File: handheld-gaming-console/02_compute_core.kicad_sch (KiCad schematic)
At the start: 2 parts, among them J3 CM4_MAIN, J4 CM4_PERIPH

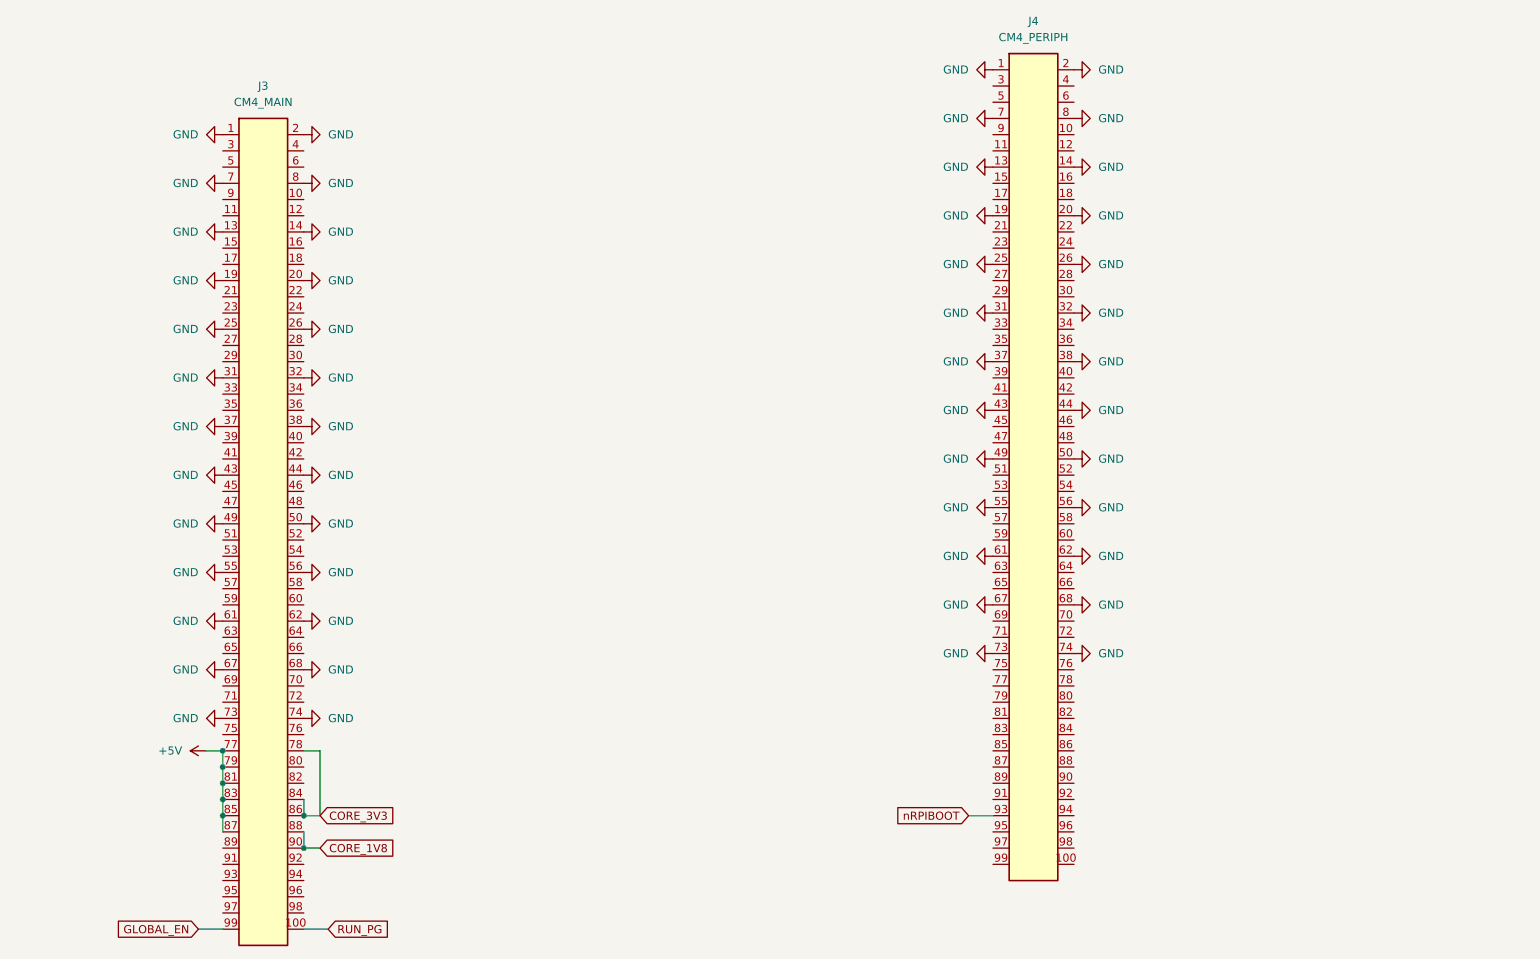
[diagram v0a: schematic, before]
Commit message: feat(usb): implement TS3USB221A high-speed mux, recovery switch, and otg role switching
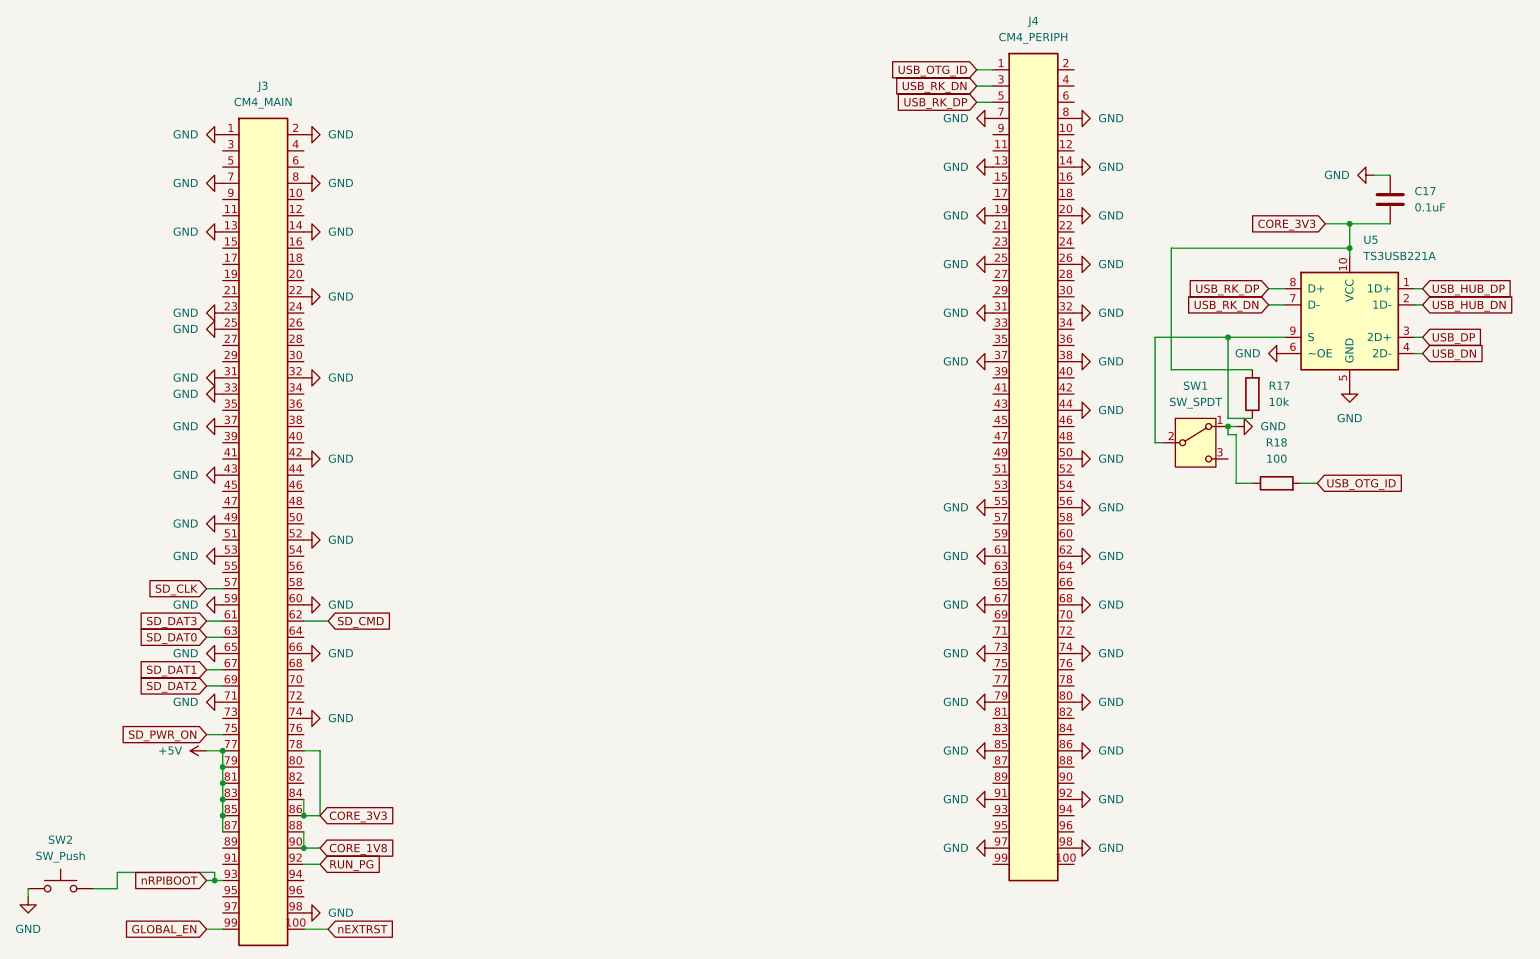
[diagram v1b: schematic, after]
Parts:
- added C17: 0.1uF, symbol Device:C
- added R17: 10k, symbol Device:R
- added R18: 100, symbol Device:R
- added SW1: SW_SPDT, Button_Switch_SMD:SW_SPDT_PCM12, symbol Switch:SW_SPDT
- added SW2: SW_Push, Button_Switch_SMD:SW_Push_SPST_NO_Alps_SKRK, symbol Switch:SW_Push
- added U5: TS3USB221A, Package_DFN_QFN:UQFN-10_1.6x2.1mm_P0.5mm, symbol custom-components:TS3USB221A
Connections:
- net CORE_3V3: now also C17.2, R17.2, U5.10 (VCC)
- net GND: now also J3.22 (Pin_22), J3.23 (Pin_23), J3.33 (Pin_33), J3.42 (Pin_42), J3.52 (Pin_52), J3.53 (Pin_53), J3.59 (Pin_59), J3.60 (Pin_60), J3.65 (Pin_65), J3.66 (Pin_66), J3.71 (Pin_71), J3.98 (Pin_98), J4.79 (Pin_79), J4.80 (Pin_80), J4.85 (Pin_85), J4.86 (Pin_86), J4.91 (Pin_91), J4.92 (Pin_92), J4.97 (Pin_97), J4.98 (Pin_98), C17.1, R18.1, SW1.1 (A), SW2.1, U5.5 (GND), U5.6 (~OE); no longer J3.19 (Pin_19), J3.20 (Pin_20), J3.26 (Pin_26), J3.38 (Pin_38), J3.44 (Pin_44), J3.50 (Pin_50), J3.55 (Pin_55), J3.56 (Pin_56), J3.61 (Pin_61), J3.62 (Pin_62), J3.67 (Pin_67), J3.68 (Pin_68), J3.73 (Pin_73), J4.1 (Pin_1), J4.2 (Pin_2), J4.43 (Pin_43), J4.49 (Pin_49)
- net RUN_PG: now also J3.92 (Pin_92); no longer J3.100 (Pin_100)
- net nRPIBOOT: now also J3.93 (Pin_93), SW2.2; no longer J4.93 (Pin_93)
- net USB_RK_DN: now reaches J4.3 (Pin_3)
- net USB_RK_DN: now also U5.7 (D-)
- net USB_RK_DP: now reaches J4.5 (Pin_5)
- net USB_RK_DP: now also U5.8 (D+)
- net SD_CLK: now reaches J3.57 (Pin_57)
- net SD_DAT0: now reaches J3.63 (Pin_63)
- net SD_DAT2: now reaches J3.69 (Pin_69)
- net SD_PWR_ON: now reaches J3.75 (Pin_75)
- new net: R17.1, SW1.2 (B), U5.9 (S)
- new net SD_CMD: J3.62 (Pin_62)
- new net SD_DAT1: J3.67 (Pin_67)
- new net SD_DAT3: J3.61 (Pin_61)
- new net USB_DN: U5.4 (2D-)
- new net USB_DP: U5.3 (2D+)
- new net USB_HUB_DN: U5.2 (1D-)
- new net USB_HUB_DP: U5.1 (1D+)
- new net USB_OTG_ID: J4.1 (Pin_1), R18.2
- new net nEXTRST: J3.100 (Pin_100)

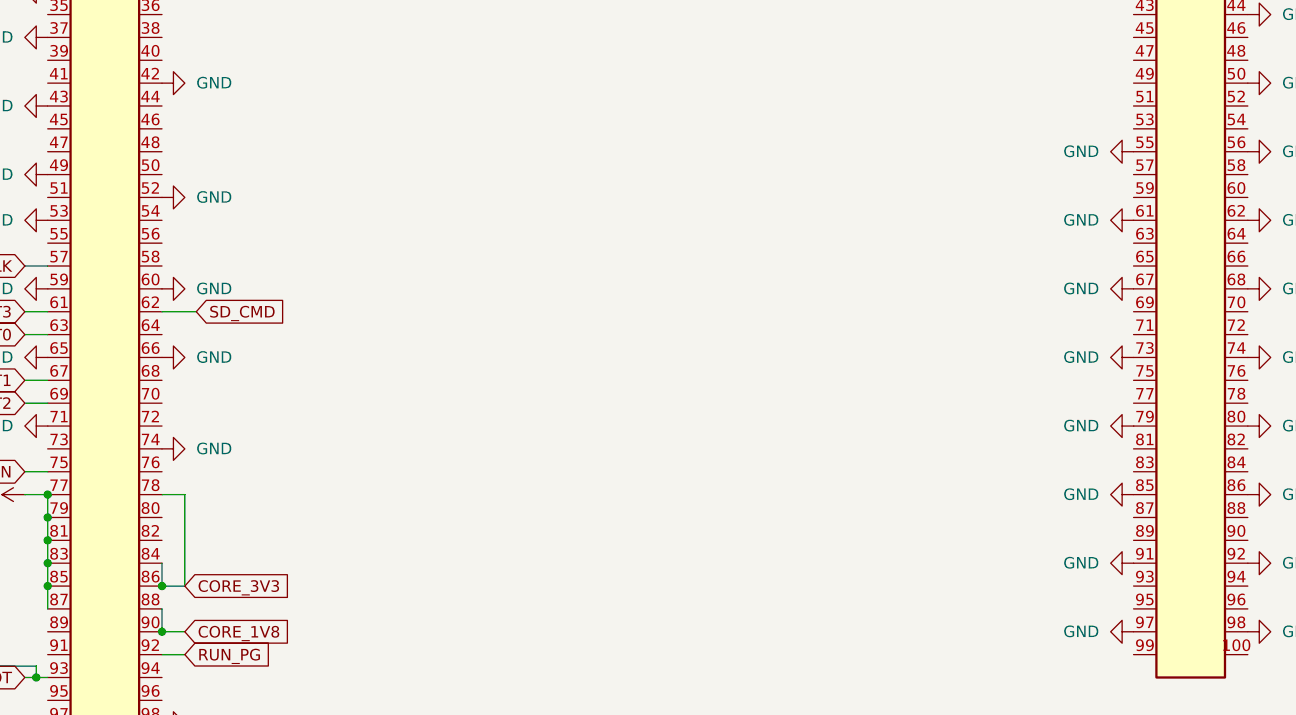
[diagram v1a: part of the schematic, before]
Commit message: feat(display): wire 15-pin FPC connector with MIPI-DSI lanes and touch I2C bus
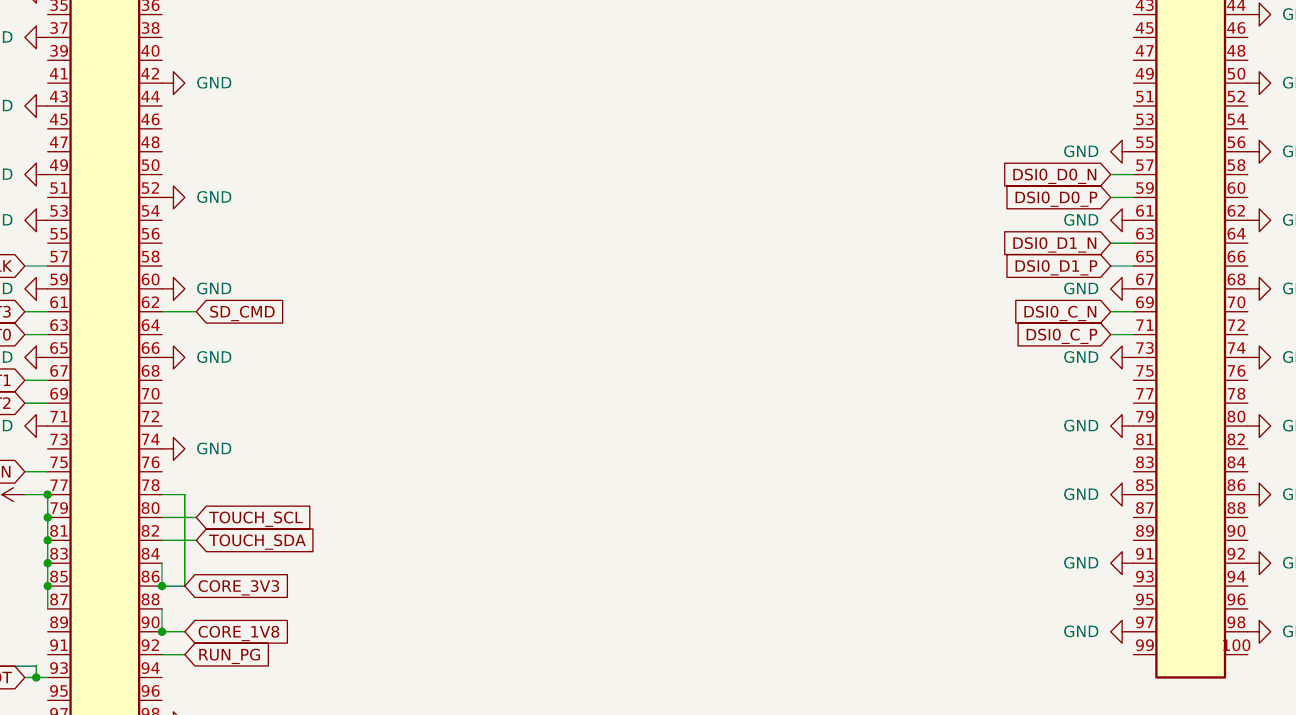
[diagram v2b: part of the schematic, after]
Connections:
- net DSI0_D0_N: now reaches J4.57 (Pin_57)
- net DSI0_D0_P: now reaches J4.59 (Pin_59)
- net DSI0_D1_N: now reaches J4.63 (Pin_63)
- net DSI0_D1_P: now reaches J4.65 (Pin_65)
- net DSI0_C_N: now reaches J4.69 (Pin_69)
- net DSI0_C_P: now reaches J4.71 (Pin_71)
- net TOUCH_SCL: now reaches J3.80 (Pin_80)
- net TOUCH_SDA: now reaches J3.82 (Pin_82)

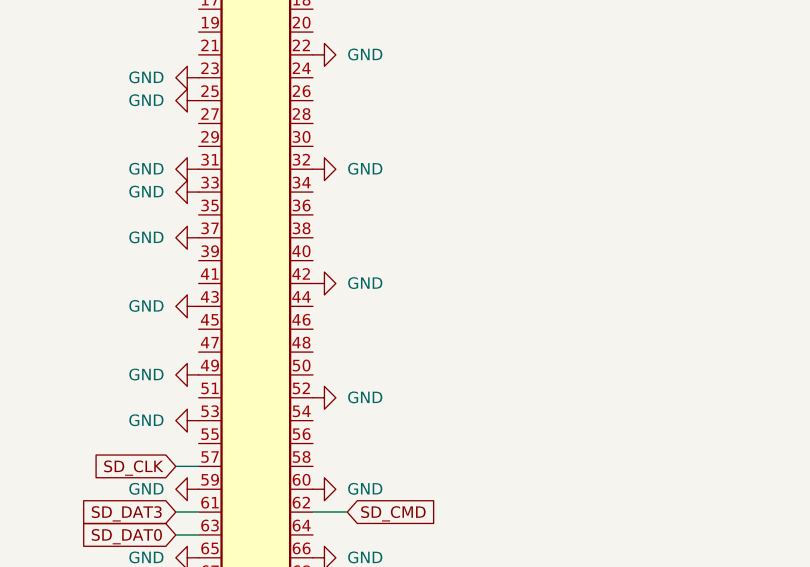
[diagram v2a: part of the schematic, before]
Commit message: feat(display): implement 3V3_LCD power switch and GT911 I2C pull-ups with address strap
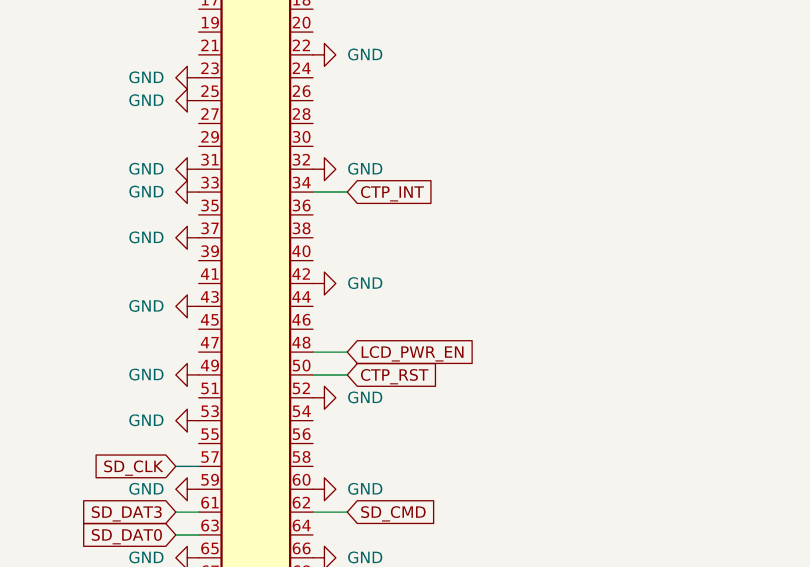
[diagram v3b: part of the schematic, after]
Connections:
- net CTP_INT: now reaches J3.34 (Pin_34)
- net LCD_PWR_EN: now reaches J3.48 (Pin_48)
- net CTP_RST: now reaches J3.50 (Pin_50)
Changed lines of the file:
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@@
+	(wire
+		(pts
+			(xy 87.63 96.52) (xy 91.44 96.52)
+		)
+		(stroke
+			(width 0)
+			(type default)
+		)
+	)
 	(wire
 		(pts
@@
 	(wire
 		(pts
+			(xy 87.63 78.74) (xy 91.44 78.74)
+		)
+		(stroke
+			(width 0)
+			(type default)
+		)
+	)
+	(wire
+		(pts
 			(xy 87.63 114.3) (xy 91.44 114.3)
 		)
@@
 	(wire
 		(pts
+			(xy 87.63 99.06) (xy 91.44 99.06)
+		)
+		(stroke
+			(width 0)
+			(type default)
+		)
+	)
+	(wire
+		(pts
 			(xy 223.52 74.93) (xy 223.52 55.88)
 		)
@@
 		)
 	)
+	(global_label "CTP_INT"
+		(shape input)
+		(at 91.44 78.74 0)
+		(fields_autoplaced yes)
+		(effects
+			(font
+				(size 1.27 1.27)
+			)
+			(justify left)
+		)
+		(property "Intersheetrefs" "${INTERSHEET_REFS}"
+			(at 101.8033 78.74 0)
+			(hide yes)
+			(show_name no)
+			(do_not_autoplace no)
+			(effects
+				(font
+					(size 1.27 1.27)
+				)
+				(justify left)
+			)
+		)
+	)
 	(global_label "CORE_3V3"
 		(shape input)
@@
 		)
 	)
+	(global_label "CTP_RST"
+		(shape input)
+		(at 91.44 99.06 0)
+		(fields_autoplaced yes)
+		(effects
+			(font
+				(size 1.27 1.27)
+			)
+			(justify left)
+		)
+		(property "Intersheetrefs" "${INTERSHEET_REFS}"
+			(at 102.3475 99.06 0)
+			(hide yes)
+			(show_name no)
+			(do_not_autoplace no)
+			(effects
+				(font
+					(size 1.27 1.27)
+				)
+				(justify left)
+			)
+		)
+	)
 	(global_label "DSI0_C_P"
 		(shape input)
@@
 			(hide yes)
 			(show_name no)
+			(do_not_autoplace no)
+			(effects
+				(font
+					(size 1.27 1.27)
+				)
+				(justify left)
+			)
+		)
+	)
+	(global_label "LCD_PWR_EN"
+		(shape input)
+		(at 91.44 96.52 0)
+		(fields_autoplaced yes)
+		(effects
+			(font
+				(size 1.27 1.27)
+			)
+			(justify left)
+		)
+		(property "Intersheetrefs" "${INTERSHEET_REFS}"
+			(at 106.3994 96.52 0)
+			(hide yes)
+			(show_name no)

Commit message: fix(core): correct J3 ground matrix, fix UART pins, add OTG_ID pull-up, and reduce BQ24075 input capacitance per design audit
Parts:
- added R33: 10k, symbol Device:R
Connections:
- net CORE_3V3: now also R33.2
- net GND: no longer J3.25 (Pin_25), J3.31 (Pin_31), J3.37 (Pin_37), J3.49 (Pin_49)
- net USB_OTG_ID: now also R33.1
- net UART2_RX: now reaches J3.51 (Pin_51)
- net UART2_TX: now reaches J3.55 (Pin_55)

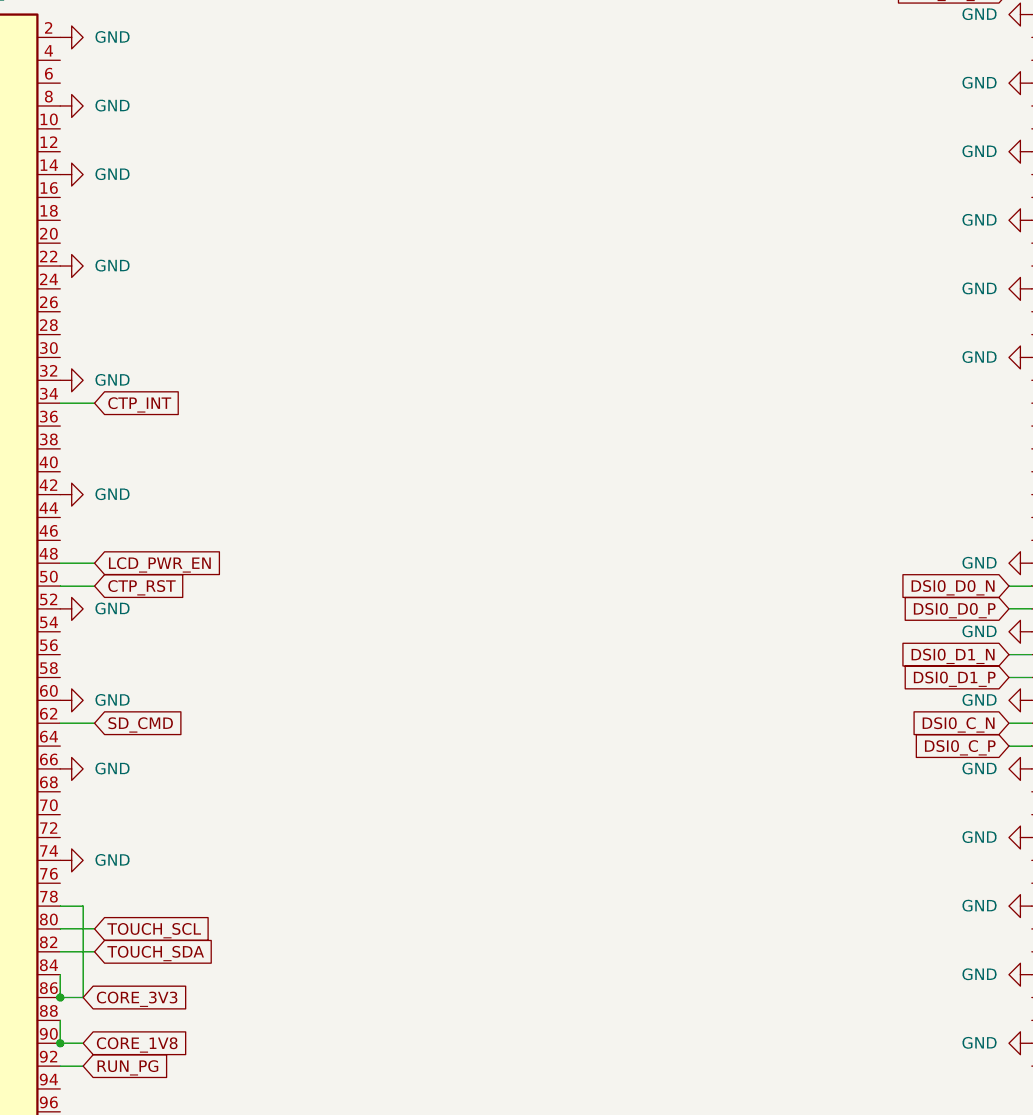
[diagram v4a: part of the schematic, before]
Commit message: feat(core): implement Rockchip-compliant MicroSD load switch, impedance damping, and ESD protection
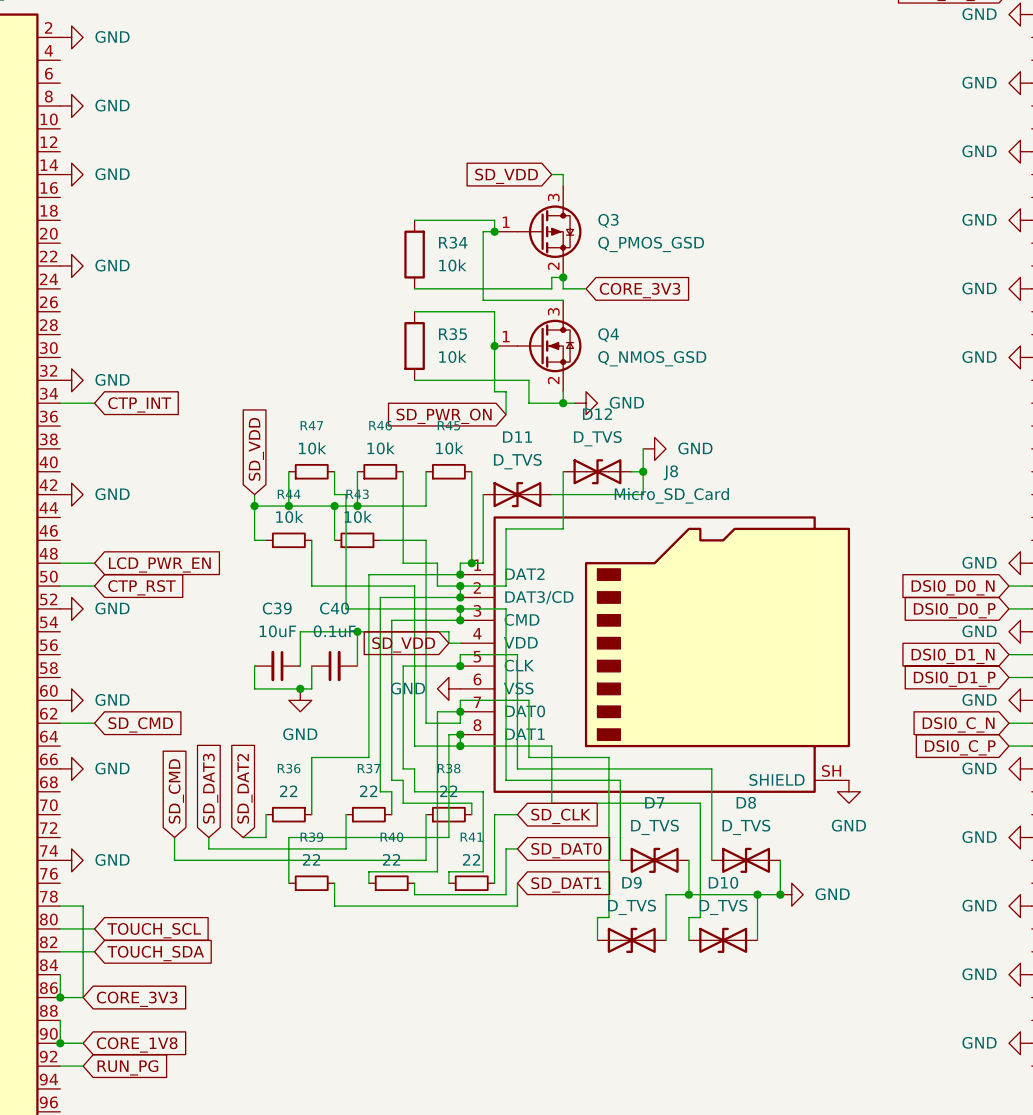
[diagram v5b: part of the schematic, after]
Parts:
- added C39: 10uF, symbol Device:C_Small
- added C40: 0.1uF, symbol Device:C_Small
- added D10, D11, D12, D7, D8, D9: D_TVS, symbol Device:D_TVS
- added J8: Micro_SD_Card, symbol Connector:Micro_SD_Card
- added Q3: Q_PMOS_GSD, symbol Transistor_FET:Q_PMOS_GSD
- added Q4: Q_NMOS_GSD, symbol Transistor_FET:Q_NMOS_GSD
- added R34, R35: 10k, symbol Device:R
- added R36, R37, R38, R39, R40, R41: 22, symbol Device:R_Small
- added R43, R44, R45, R46, R47: 10k, symbol Device:R_Small
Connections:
- net CORE_3V3: now also Q3.2 (S), R34.1
- net GND: now also C39.2, C40.1, D10.2 (A2), D11.2 (A2), D12.2 (A2), D7.2 (A2), D8.2 (A2), D9.2 (A2), J8.6 (VSS), J8.SH (SHIELD), Q4.2 (S), R35.2
- net SD_CLK: now also R41.2
- net SD_CMD: now also R38.1
- net SD_DAT0: now also R40.2
- net SD_DAT1: now also R39.2
- net SD_DAT2: now also R36.2
- net SD_DAT3: now also R37.1
- net SD_PWR_ON: now also Q4.1 (G), R35.1
- new net: D9.1 (A1), J8.7 (DAT0), R40.1, R43.2
- new net: Q3.1 (G), Q4.3 (D), R34.2
- new net: D7.1 (A1), J8.3 (CMD), R38.2, R47.2
- new net: D11.1 (A1), J8.1 (DAT2), R36.1, R45.2
- new net: D12.1 (A1), J8.2 (DAT3/CD), R37.2, R46.2
- new net: D8.1 (A1), J8.5 (CLK), R41.1
- new net: D10.1 (A1), J8.8 (DAT1), R39.1, R44.2
- new net SD_VDD: C39.1, C40.2, J8.4 (VDD), Q3.3 (D), R43.1, R44.1, R45.1, R46.1, R47.1
